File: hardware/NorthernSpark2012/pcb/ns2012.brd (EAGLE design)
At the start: 35.2 x 35.5 mm, 12 parts, among them IC1 TINY24/44/84-SSU, J1 AVR_SPI_PRG_6NS

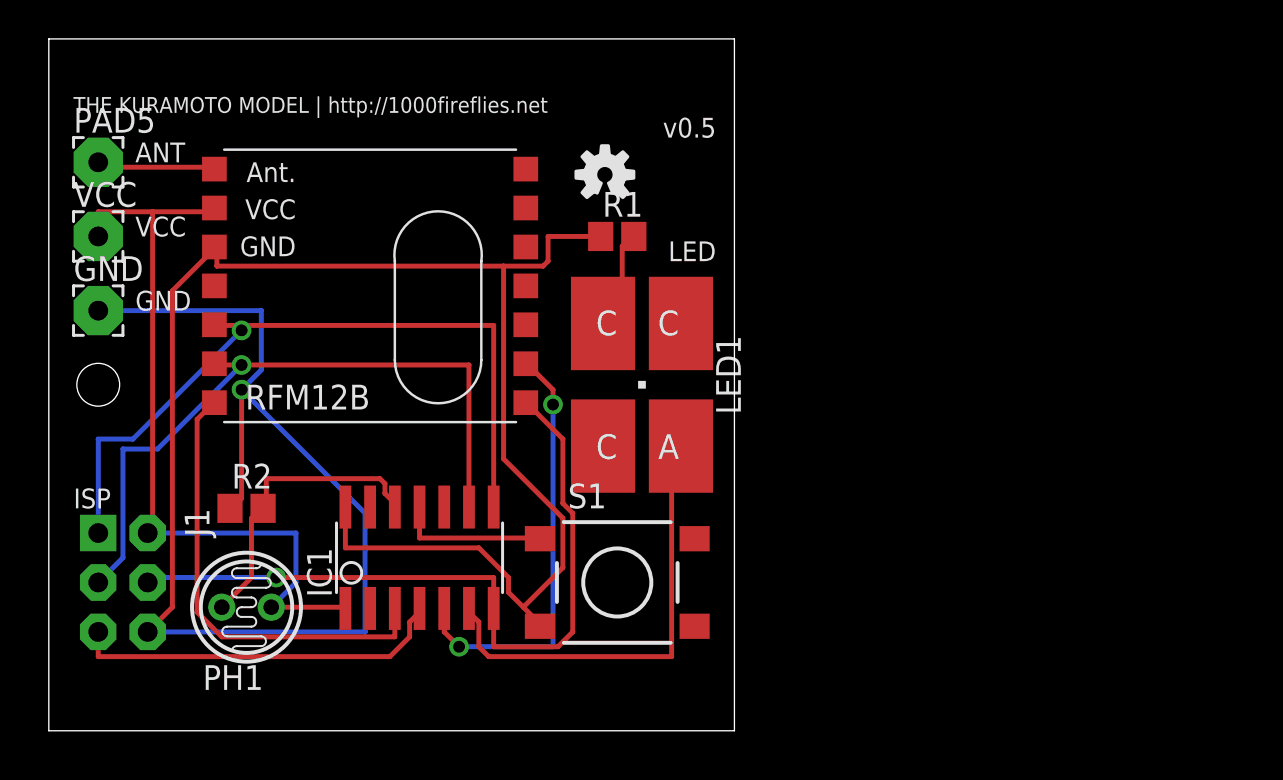
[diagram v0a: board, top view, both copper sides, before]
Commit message: Removed old revisions and added two new ones. General repo cleanup.
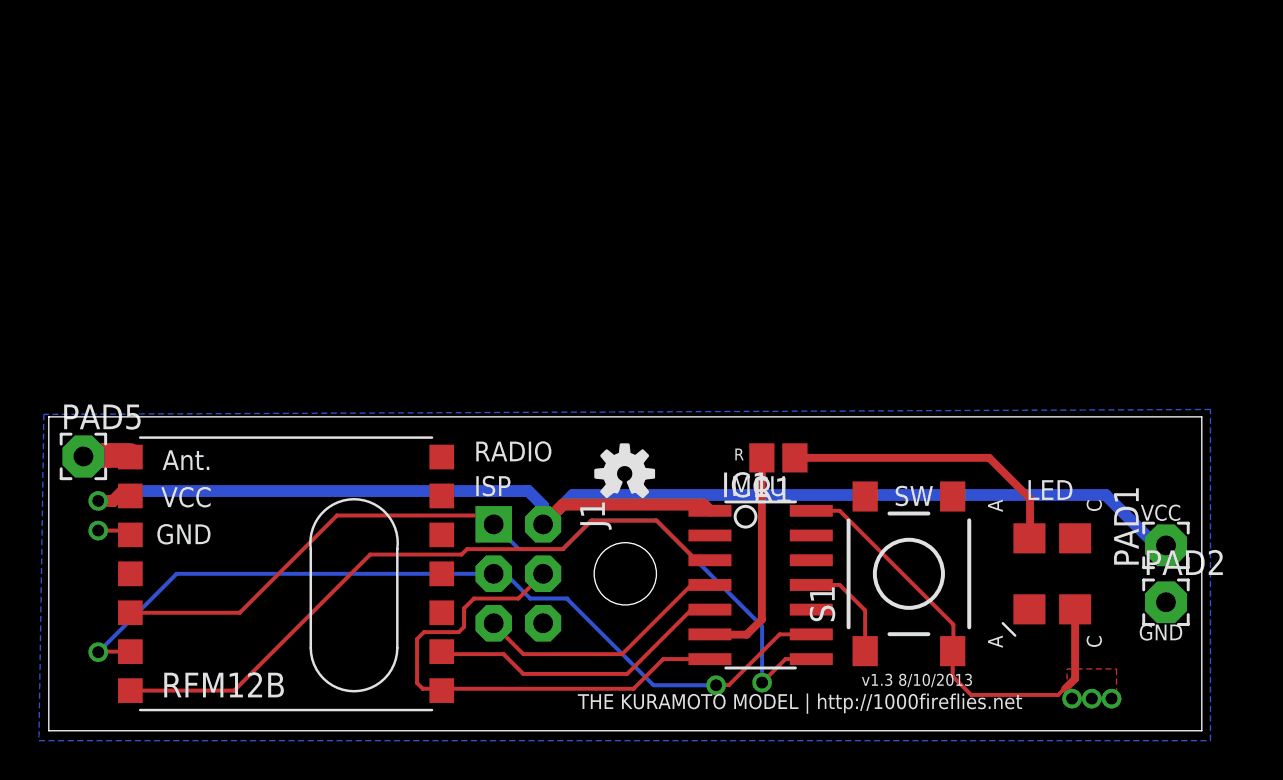
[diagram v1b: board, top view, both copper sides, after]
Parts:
- removed GND: GND, wirepad:2,54/1,0
- removed LED1: CLM4B-RKW-CWaXbAA3, led:P-LCC-4
- removed PH1: VT20N1, photo-elements:TO46-VT200
- removed R2: (no value), resistor:R0805
- removed VCC: VCC, wirepad:2,54/1,0
- added PAD1: VCC, wirepad:2,15/1,0
- added PAD2: GND, wirepad:2,15/1,0
- added U$3: Avago 630-ALMD-EG3D-VX002, ALMD-XX3D:ALMD-**3D
- IC1: value TINY24/44/84-SSU -> Atmel ATtiny84a-SSU
- PAD5: device wirepad:2,54/1,0 -> wirepad:2,15/1,0
- R1: value 18 ohm -> 30 ohm
- RFM12B: value RFM12BN -> HopeRF RFM12B-433S1
- S1: value DTSM-6 -> Mountain Switch 101-0364-EV
- moved J1 20.3 mm to (24.1, 8.06)
- moved IC1 17.6 mm to (36.6, 7.49), turned to 270 degrees
- moved RFM12B 15.4 mm to (12.2, 8.06)
- moved U$1 15.4 mm to (29.6, 13.2)
- moved PAD5 15.1 mm to (1.78, 14.1)
- moved S1 15.0 mm to (44.2, 8.06), turned to 90 degrees
- moved R1 14.1 mm to (37.5, 14.0), turned to 180 degrees
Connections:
- removed net N$9: IC1.12, PH1.1, R2.2
- net GND: now also PAD2.1, U$3.C1, U$3.C2; no longer GND.1, R1.1, R2.1
- net N$1: now also R1.1, U$3.A1, U$3.A2; no longer LED1.C@4, R1.2
- net N$6: now also R1.2; no longer LED1.A
- net VCC: now also PAD1.1; no longer PH1.2, VCC.1
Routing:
- net GND: track 122.8 -> 25.8 mm, vias 1 -> 4
- net VCC: track 39.9 -> 69.5 mm, vias 0 -> 1
- net N$9: track 15.3 -> 0.00 mm
- net N$6: track 23.3 -> 11.3 mm
- net N$4: track 38.6 -> 26.6 mm, vias 1 -> 0
- net N$5: track 23.3 -> 34.2 mm
- net N$1: track 5.20 -> 15.0 mm
- net N$2: track 35.7 -> 43.8 mm, vias 1 -> 2
- net N$7: track 22.3 -> 15.6 mm, vias 2 -> 0
- net N$14: track 19.4 -> 13.3 mm
- net N$3: track 38.4 -> 44.0 mm
- net N$8: track 6.26 -> 2.48 mm
- net N$10: track 7.78 -> 5.40 mm
- added copper zone on layer 1, net GND
- added copper zone on layer 16, net GND
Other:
- board size 35.2 x 35.5 mm -> 59.2 x 16.1 mm
- board text added: "MCU"
- board text added: "R"
- board text added: "RADIO"
- board text added: "SW"
- board text added: "v1.3 8/10/2013"
- board text removed: "ANT"
- board text removed: "v0.5"
